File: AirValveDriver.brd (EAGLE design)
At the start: 71.1 x 62.2 mm, 16 parts, among them IC2 NE555, Q1 2N2222, Q2 STF40NF06

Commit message: updated after DRC
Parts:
- added DRILEGEND: (no value), drilegend:DRILEGEND
- C1: device resistor:C025-030X050 -> myDevices:CPOL_PKG
- C2, C4: value 10u -> CAPACITOR_POLARIZED; device resistor:C025-030X050 -> myDevices:CPOL_PKG
- C3: value 0.1u -> CAPACITOR_POLARIZED; device resistor:C025-030X050 -> myDevices:CPOL_PKG
- IC1: value (none) -> LM7805
- Q1: device transistor-npn:TO18 -> myDevices:TO18
- R1, R2, R3, R4, R5: device resistor:0207/10 -> myDevices:RESISTOR_PKG
- moved R5 32.1 mm to (34.3, 55.9)
- moved C2 23.4 mm to (54.6, 49.5)
- moved C1 17.1 mm to (34.3, 43.2), turned to 270 degrees
- moved C4 10.9 mm to (24.1, 43.2)
- moved Q1 7.41 mm to (41.9, 49.5), turned to 0 degrees
- moved IC1 6.84 mm to (25.4, 53.3)
- moved C3 6.35 mm to (50.8, 27.9), turned to 180 degrees
- moved R1 5.39 mm to (33.0, 31.8)
- moved R2 5.08 mm to (33.0, 25.4)
- moved R3 4.02 mm to (40.6, 38.1)
- moved Q2 3.59 mm to (48.3, 61.0)
- moved R4 2.84 mm to (59.7, 43.2)
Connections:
- net +5V: now also C4.+; no longer C4.1
- net AGND: now also C2.-, C3.-, C4.-, R2.1; no longer C2.2, C3.2, C4.2, R2.2
- net N$1: now also C3.+; no longer C3.1
- net N$10: now also C2.+; no longer C2.1
- net N$5: now also C1.+; no longer C1.1
- net N$6: now also C1.-, R2.2; no longer C1.2, R2.1
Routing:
- net N$4: track 33.9 -> 57.1 mm
- net N$5: track 19.6 -> 39.3 mm
- net N$2: track 29.6 -> 12.0 mm
- net N$7: track 11.2 -> 27.9 mm, vias 0 -> 2
- net +5V: track 71.7 -> 59.7 mm
- net N$6: track 24.0 -> 35.2 mm, vias 0 -> 2
- net OUTPUT_1: track 19.4 -> 23.2 mm
- net N$10: track 22.6 -> 25.3 mm
- net N$1: track 6.13 -> 7.37 mm
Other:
- board size 71.1 x 62.2 mm -> 70.8 x 59.7 mm
- board text added: "01-16"
- board text added: "01-20"
- board text added: "LAYER-STACK"

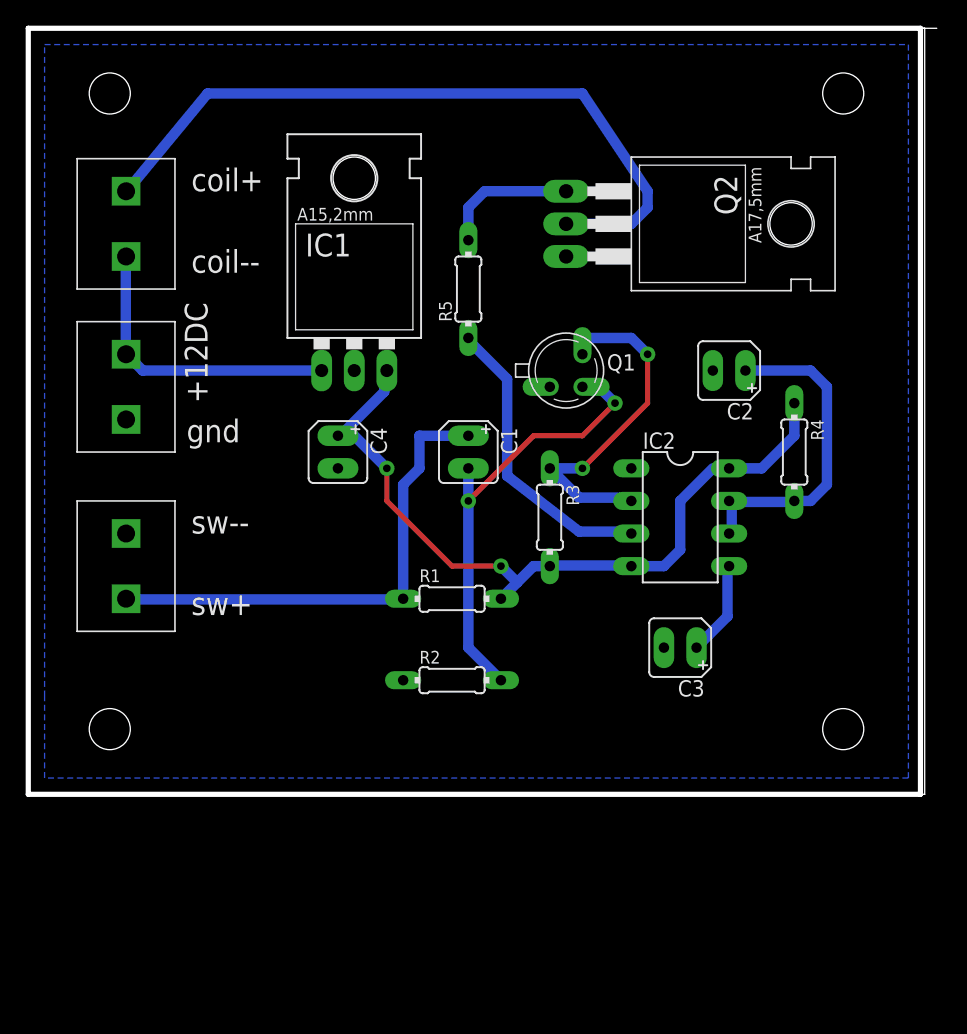
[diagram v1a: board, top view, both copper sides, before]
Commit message: mod board to use compliant drills
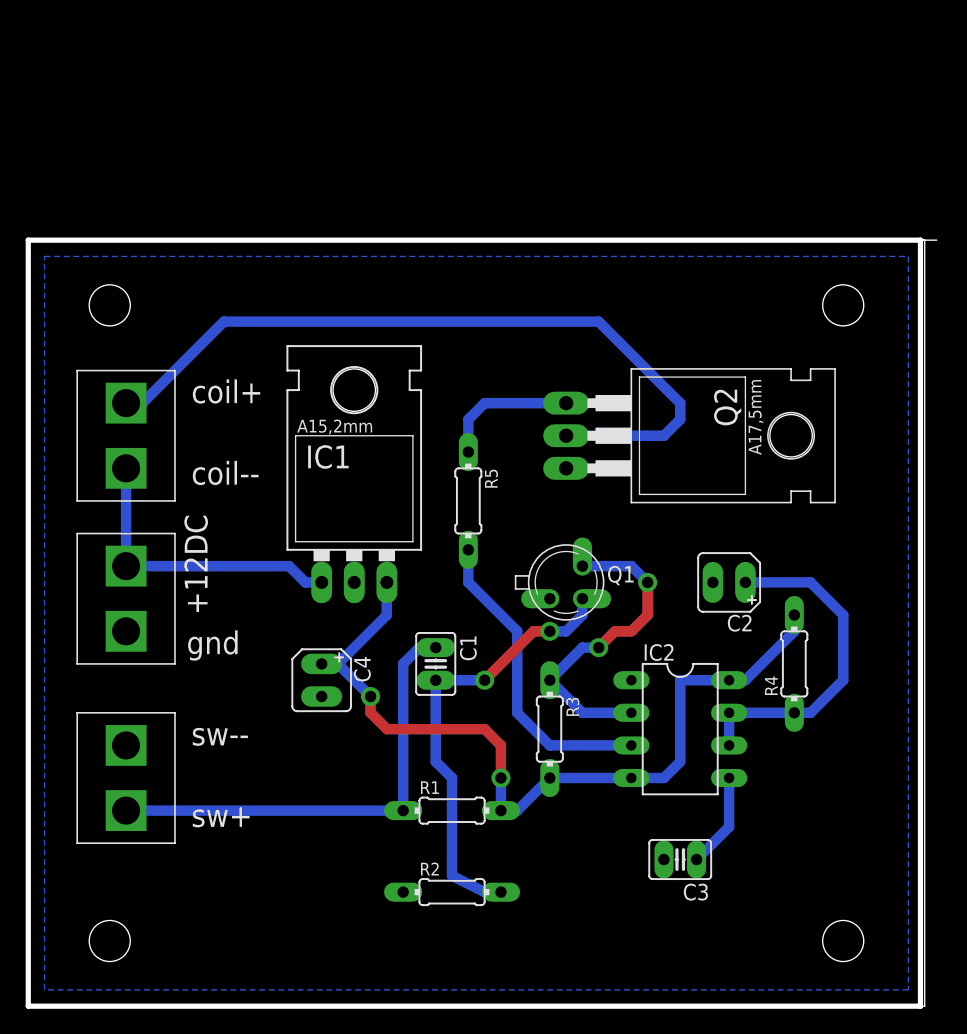
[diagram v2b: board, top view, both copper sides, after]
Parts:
- removed POWER_IN: PWR_IN, myLibrary:TB2_PKG
- added U$5: TB2, myDevices:TB2_PKG
- C1: device myDevices:CPOL_PKG -> myDevices:CCERAMIC_PKG
- C2, C4: value CAPACITOR_POLARIZED -> 10u
- C3: value CAPACITOR_POLARIZED -> 0.1u; device myDevices:CPOL_PKG -> myDevices:CCERAMIC_PKG
- R4: value 51k -> 10k
- R5: value 100 -> 10k
- U$2: value Air Valve -> TB2; device myLibrary:TB2_PKG -> myDevices:TB2_PKG
- U$3: value switch -> Pwr; device myLibrary:TB2_PKG -> myDevices:TB2_PKG
- moved C4 17.8 mm to (22.9, 25.4)
- moved C1 16.7 mm to (31.8, 26.7)
- moved IC1 16.5 mm to (25.4, 36.8)
- moved R5 16.5 mm to (34.3, 39.4), turned to 270 degrees
- moved C3 16.5 mm to (50.8, 11.4)
- moved IC2 16.5 mm to (50.8, 21.6)
- moved R3 16.5 mm to (40.6, 21.6)
- moved C2 16.5 mm to (54.6, 33.0)
- moved DRILEGEND 16.5 mm to (-0.20, -10.9)
- moved Q1 16.5 mm to (41.9, 33.0)
- moved Q2 16.5 mm to (48.3, 44.5)
- moved R1 16.5 mm to (33.0, 15.2)
- moved R2 16.5 mm to (33.0, 8.89)
- moved R4 16.5 mm to (59.7, 26.7), turned to 90 degrees
- moved U$2 16.5 mm to (7.62, 44.5)
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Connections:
- net +12V: now also U$3.P$2; no longer POWER_IN.P$2
- net +5V: now also R4.2; no longer R4.1
- net AGND: now also C3.2, U$5.P$1; no longer C3.-, POWER_IN.P$1
- net N$1: now also C3.1; no longer C3.+
- net N$10: now also R4.1; no longer R4.2
- net N$2: now also R5.1; no longer R5.2
- net N$5: now also C1.1, U$5.P$2; no longer C1.+, U$3.P$2
- net N$6: now also C1.2; no longer C1.-
- net OUTPUT_1: now also R5.2; no longer R5.1
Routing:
- net +5V: track 59.7 -> 64.0 mm
- net N$5: track 39.3 -> 36.1 mm
- net N$7: track 27.9 -> 25.3 mm
- net N$4: track 57.1 -> 59.1 mm
- net N$2: track 12.0 -> 10.7 mm
- net OUTPUT_1: track 23.2 -> 24.2 mm
- net N$10: track 25.3 -> 26.2 mm
- net N$6: track 35.2 -> 34.7 mm

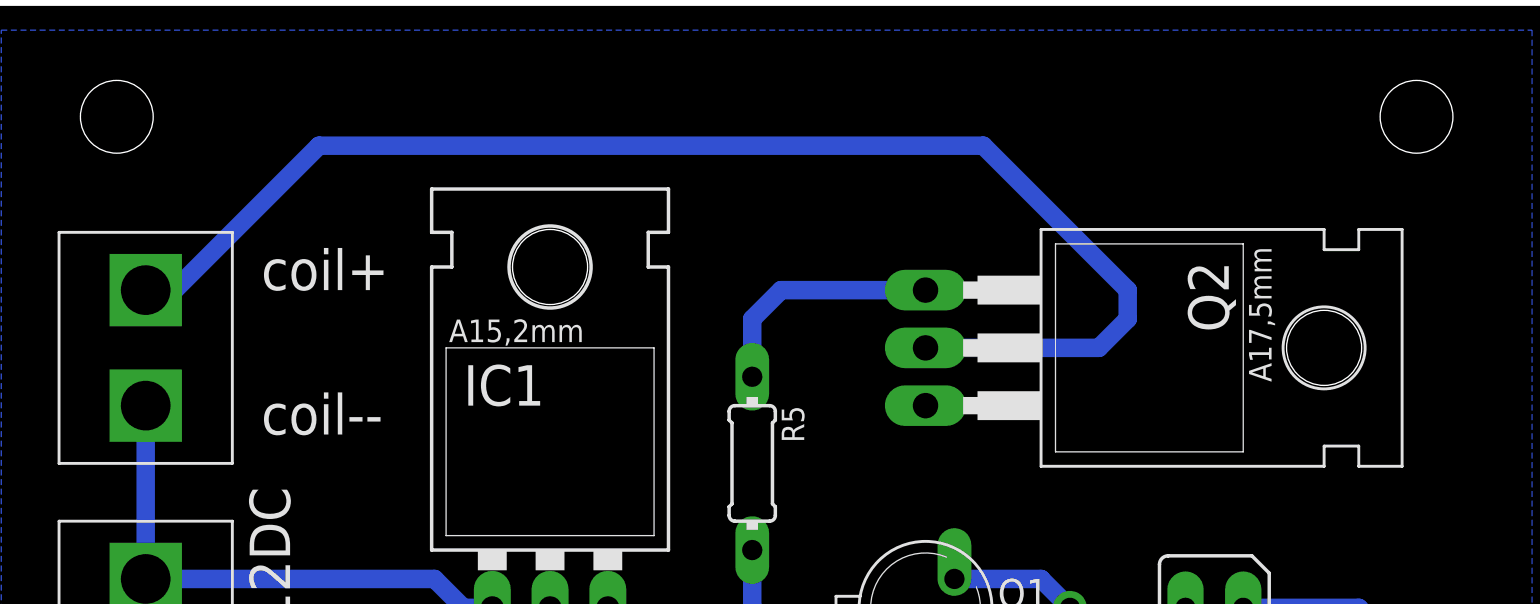
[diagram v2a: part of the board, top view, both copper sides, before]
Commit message: updated cam files to run a copy of the board
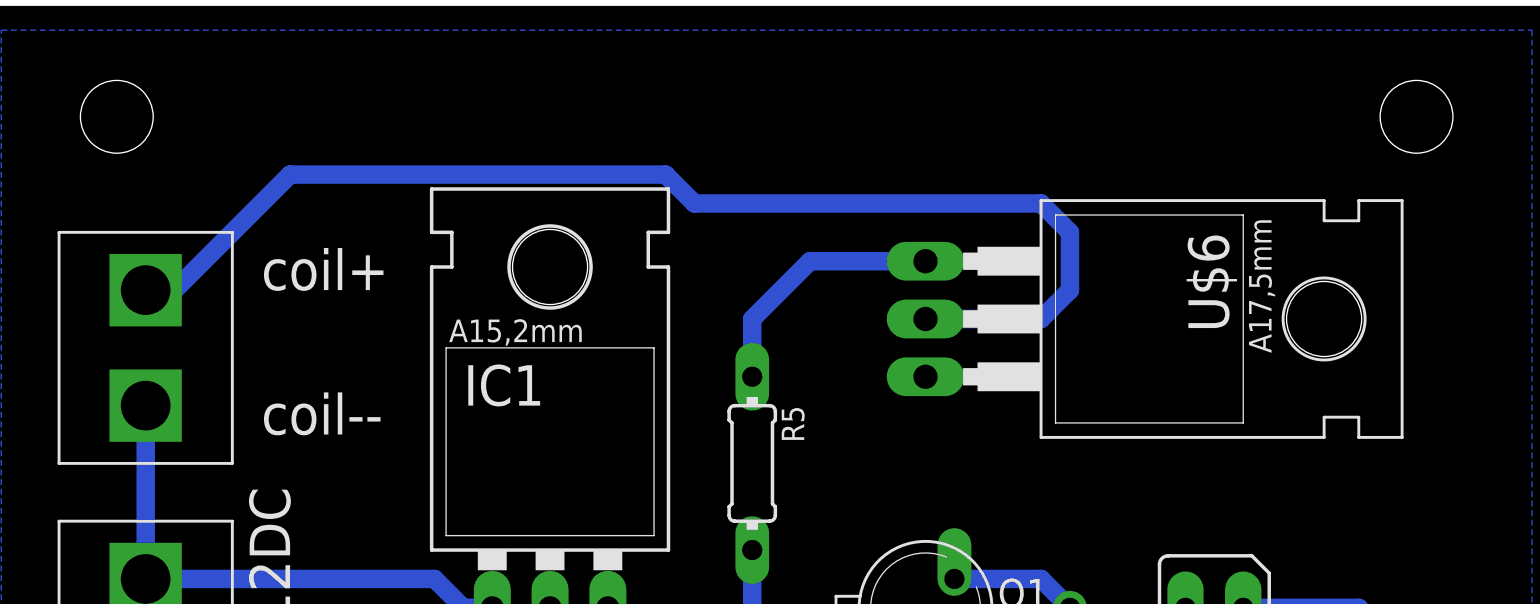
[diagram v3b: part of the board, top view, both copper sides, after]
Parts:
- removed DRILEGEND: (no value), drilegend:DRILEGEND
- removed Q2: STF40NF06, transistor-fet:TO220
- added U$6: STF40NF06, myDevices:TO220H
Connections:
- removed net N$4: Q2.2, U$2.P$2
- new net N$3: U$2.P$2, U$6.2
- net AGND: now also U$6.3; no longer Q2.3
- net N$2: now also U$6.1; no longer Q2.1
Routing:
- net N$4: track 59.1 -> 0.00 mm
- net N$3: track 0.00 -> 53.2 mm
- net N$2: track 10.7 -> 11.2 mm
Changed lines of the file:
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@@
 <elements>
 <element name="IC1" library="v-reg" package="78XXL" value="LM7805" x="25.4" y="36.83"/>
-<element name="Q2" library="transistor-fet" package="TO220" value="STF40NF06" x="48.26" y="44.45" smashed="yes" rot="R270">
-<attribute name="NAME" x="53.467" y="48.26" size="1.778" layer="25" ratio="10" rot="R270"/>
-<attribute name="VALUE" x="45.593" y="36.83" size="1.778" layer="27" ratio="10"/>
-</element>
 <element name="IC2" library="st-microelectronics" package="DIL-08" value="NE555" x="50.8" y="21.59" rot="R270">
 <attribute name="OC_NEWARK" value="89K1486" x="44.45" y="-20.32" size="1.778" layer="27" rot="R270" display="off"/>
@@
 <element name="U$5" library="myDevices" package="TB2_PKG" value="TB2" x="7.62" y="17.78"/>
 <element name="U$2" library="myDevices" package="TB2_PKG" value="TB2" x="7.62" y="44.45" rot="R180"/>
-<element name="DRILEGEND" library="drilegend" package="DRILEGEND" value="" x="-0.2032" y="-10.90500625"/>
+<element name="U$6" library="myDevices" package="TO220H" value="STF40NF06" x="53.34" y="45.72" rot="R270"/>
 </elements>
 <signals>
@@
 <contactref element="IC1" pad="GND"/>
 <contactref element="IC2" pad="1"/>
-<contactref element="Q2" pad="3"/>
 <contactref element="Q1" pad="1"/>
 <contactref element="R2" pad="1"/>
@@
 <vertex x="1.27" y="1.27"/>
 </polygon>
+<contactref element="U$6" pad="3"/>
 </signal>
 <signal name="+5V">
@@
 <wire x1="34.29" y1="33.02" x2="34.29" y2="35.56" width="0.8128" layer="16"/>
 </signal>
-<signal name="N$4">
-<contactref element="Q2" pad="2"/>
-<contactref element="U$2" pad="P$2"/>
-<wire x1="7.62" y1="46.99" x2="8.89" y2="46.99" width="0.8128" layer="16"/>
-<wire x1="8.89" y1="46.99" x2="15.24" y2="53.34" width="0.8128" layer="16"/>
-<wire x1="15.24" y1="53.34" x2="44.45" y2="53.34" width="0.8128" layer="16"/>
-<wire x1="44.45" y1="53.34" x2="50.8" y2="46.99" width="0.8128" layer="16"/>
-<wire x1="50.8" y1="46.99" x2="50.8" y2="45.72" width="0.8128" layer="16"/>
-<wire x1="50.8" y1="45.72" x2="49.53" y2="44.45" width="0.8128" layer="16"/>
-<wire x1="49.53" y1="44.45" x2="41.91" y2="44.45" width="0.8128" layer="16"/>
-</signal>
 <signal name="N$2">
-<contactref element="Q2" pad="1"/>
 <contactref element="R5" pad="1"/>
 <wire x1="34.29" y1="43.18" x2="34.29" y2="45.72" width="0.8128" layer="16"/>
-<wire x1="34.29" y1="45.72" x2="35.56" y2="46.99" width="0.8128" layer="16"/>
-<wire x1="35.56" y1="46.99" x2="41.91" y2="46.99" width="0.8128" layer="16"/>
+<contactref element="U$6" pad="1"/>
+<wire x1="41.91" y1="48.26" x2="36.83" y2="48.26" width="0.8128" layer="16"/>
+<wire x1="36.83" y1="48.26" x2="34.29" y2="45.72" width="0.8128" layer="16"/>
+</signal>
+<signal name="N$3">
+<contactref element="U$6" pad="2"/>
+<contactref element="U$2" pad="P$2"/>
+<wire x1="41.91" y1="45.72" x2="46.99" y2="45.72" width="0.8128" layer="16"/>
+<wire x1="46.99" y1="45.72" x2="48.26" y2="46.99" width="0.8128" layer="16"/>
+<wire x1="48.26" y1="46.99" x2="48.26" y2="49.53" width="0.8128" layer="16"/>
+<wire x1="48.26" y1="49.53" x2="46.99" y2="50.8" width="0.8128" layer="16"/>
+<wire x1="46.99" y1="50.8" x2="31.75" y2="50.8" width="0.8128" layer="16"/>
+<wire x1="31.75" y1="50.8" x2="30.48" y2="52.07" width="0.8128" layer="16"/>
+<wire x1="30.48" y1="52.07" x2="13.97" y2="52.07" width="0.8128" layer="16"/>
+<wire x1="13.97" y1="52.07" x2="8.89" y2="46.99" width="0.8128" layer="16"/>
+<wire x1="8.89" y1="46.99" x2="7.62" y2="46.99" width="0.8128" layer="16"/>
 </signal>
 </signals>
